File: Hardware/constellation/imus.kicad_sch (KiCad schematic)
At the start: 8 parts, among them U2 ICM-45686, U3 LSM6DSV32X

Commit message: shift to hierarchial design, add GNSS, mag, accel
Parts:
- removed C1, C2, C3, C4: 100nF, Capacitor_SMD:C_0402_1005Metric, symbol Device:C_Small
- removed R1, R2: 10K, Resistor_SMD:R_0402_1005Metric_Pad0.72x0.64mm_HandSolder, symbol Device:R_Small
- removed U2: ICM-45686, ICM_45686:IC_ICM-45686, symbol ICM-45686:ICM-45686
- removed U3: LSM6DSV32X, Package_LGA:LGA-14_3x2.5mm_P0.5mm_LayoutBorder3x4y, symbol Sensor_Motion:LSM6DSL
- added C16, C17, C18, C19: 100nF, Capacitor_SMD:C_0402_1005Metric, symbol Device:C_Small
- added R11, R12: 10K, Resistor_SMD:R_0402_1005Metric_Pad0.72x0.64mm_HandSolder, symbol Device:R_Small
- added U11: ICM-45686, ICM_45686:IC_ICM-45686, symbol ICM-45686:ICM-45686
- added U12: LSM6DSV32X, Package_LGA:LGA-14_3x2.5mm_P0.5mm_LayoutBorder3x4y, symbol Sensor_Motion:LSM6DSL
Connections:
- net GND: now also C16.2, C17.2, C18.2, C19.2, U11.10 (RESV), U11.11 (RESV), U11.2 (RESV), U11.3 (RESV), U11.6 (GND), U11.7 (RESV), U12.2 (SDX), U12.3 (SCX), U12.6 (GND), U12.7 (GND)
- net ICM_CS: now also R12.2, U11.12 (AP_CS)
- net ICM_INT1: now also U11.4 (INT1/INT), U12.4 (INT1)
- net ICM_INT2: now also U11.9 (INT2/CLKIN), U12.9 (INT2)
- net ICM_MISO: now also U11.1 (AP_SDO)
- net ICM_MOSI: now also U11.14 (AP_SDIO/AP_SDI)
- net ICM_SCK: now also U11.13 (AP_SCLK)
- net LSM6_CS: now also R11.2, U12.12 (CS)
- net LSM6_MISO: now also U12.1 (SDO/SA0)
- net LSM6_MOSI: now also U12.14 (SDA)
- net LSM6_SCK: now also U12.13 (SCL)
- net VDD: now also C16.1, C17.1, C18.1, C19.1, R11.1, R12.1, U11.5 (VDDIO), U11.8 (VDD), U12.5 (VDDIO), U12.8 (VDD)

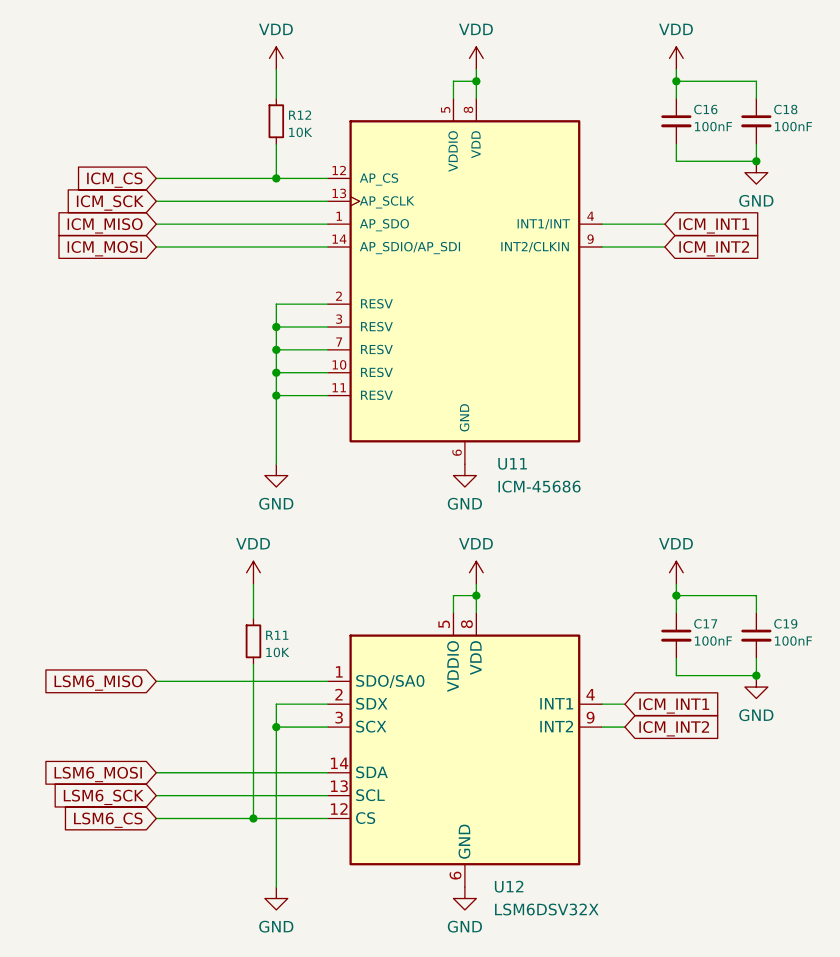
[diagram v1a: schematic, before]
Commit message: add the hierarchal pins to the imu block
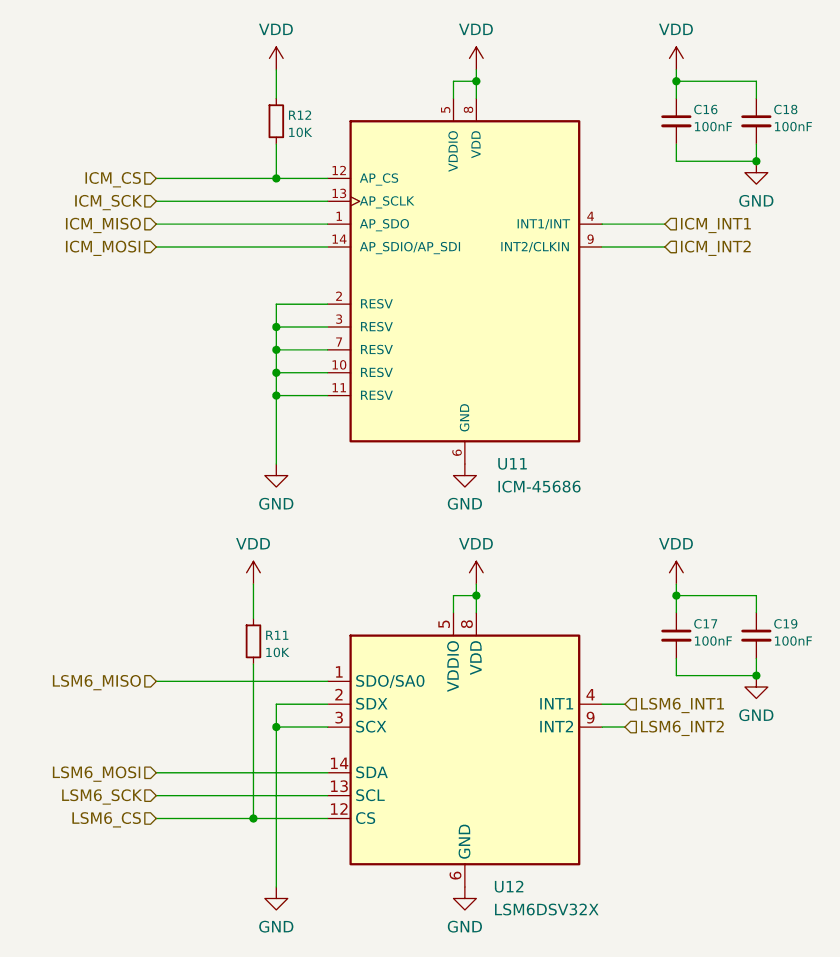
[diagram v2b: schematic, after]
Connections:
- net ICM_INT1: no longer U12.4 (INT1)
- net ICM_INT2: no longer U12.9 (INT2)
- new net LSM6_INT1: U12.4 (INT1)
- new net LSM6_INT2: U12.9 (INT2)
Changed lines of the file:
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@@
 		)
 	)
-	(global_label "ICM_SCK"
+	(hierarchical_label "ICM_SCK"
 		(shape input)
 		(at 113.03 73.66 180)
-		(fields_autoplaced yes)
 		(effects
 			(font
@@
 			(justify right)
 		)
-		(property "Intersheetrefs" "${INTERSHEET_REFS}"
-			(at 94.0187 73.66 0)
-			(hide yes)
-			(show_name no)
-			(do_not_autoplace no)
-			(effects
-				(font
-					(size 1.27 1.27)
-				)
-				(justify right)
-			)
-		)
 	)
-	(global_label "LSM6_SCK"
+	(hierarchical_label "LSM6_SCK"
 		(shape input)
 		(at 113.03 139.7 180)
-		(fields_autoplaced yes)
 		(effects
 			(font
@@
 			(justify right)
 		)
-		(property "Intersheetrefs" "${INTERSHEET_REFS}"
-			(at 94.0187 139.7 0)
-			(hide yes)
-			(show_name no)
-			(do_not_autoplace no)
-			(effects
-				(font
-					(size 1.27 1.27)
-				)
-				(justify right)
-			)
-		)
 	)
-	(global_label "ICM_INT2"
+	(hierarchical_label "LSM6_INT2"
 		(shape input)
-		(at 169.545 78.74 0)
-		(fields_autoplaced yes)
+		(at 165.1 132.08 0)
 		(effects
 			(font
@@
 			(justify left)
 		)
-		(property "Intersheetrefs" "${INTERSHEET_REFS}"
-			(at 188.5563 78.74 0)
-			(hide yes)
-			(show_name no)
-			(do_not_autoplace no)
-			(effects
-				(font
-					(size 1.27 1.27)
-				)
-				(justify left)
-			)
-		)
 	)
-	(global_label "LSM6_MISO"
+	(hierarchical_label "ICM_MOSI"
 		(shape input)
-		(at 113.03 127 180)
-		(fields_autoplaced yes)
+		(at 113.03 78.74 180)
 		(effects
 			(font
@@
 			(justify right)
 		)
-		(property "Intersheetrefs" "${INTERSHEET_REFS}"
-			(at 94.0187 127 0)
-			(hide yes)
-			(show_name no)
-			(do_not_autoplace no)
-			(effects
-				(font
-					(size 1.27 1.27)
-				)
-				(justify right)
-			)
-		)
 	)
-	(global_label "ICM_MOSI"
+	(hierarchical_label "LSM6_MOSI"
 		(shape input)
-		(at 113.03 78.74 180)
-		(fields_autoplaced yes)
+		(at 113.03 137.16 180)
 		(effects
 			(font
@@
 			(justify right)
 		)
-		(property "Intersheetrefs" "${INTERSHEET_REFS}"
-			(at 94.0187 78.74 0)
-			(hide yes)
-			(show_name no)
-			(do_not_autoplace no)
-			(effects
-				(font
-					(size 1.27 1.27)
-				)
-				(justify right)
+	)
+	(hierarchical_label "ICM_CS"
+		(shape input)
+		(at 113.03 71.12 180)
+		(effects
+			(font
+				(size 1.27 1.27)
 			)
+			(justify right)
 		)
 	)
-	(global_label "ICM_INT1"
+	(hierarchical_label "LSM6_INT1"
 		(shape input)
-		(at 169.545 76.2 0)
-		(fields_autoplaced yes)
+		(at 165.1 129.54 0)
 		(effects
 			(font
@@
 			(justify left)
 		)
-		(property "Intersheetrefs" "${INTERSHEET_REFS}"
-			(at 188.5563 76.2 0)
-			(hide yes)
-			(show_name no)
-			(do_not_autoplace no)
-			(effects
-				(font
-					(size 1.27 1.27)
-				)
-				(justify left)
+	)
+	(hierarchical_label "ICM_INT1"
+		(shape input)
+		(at 169.545 76.2 0)
+		(effects
+			(font
+				(size 1.27 1.27)
 			)
+			(justify left)
 		)
 	)
-	(global_label "LSM6_CS"
+	(hierarchical_label "ICM_MISO"
 		(shape input)
-		(at 113.03 142.24 180)
-		(fields_autoplaced yes)
+		(at 113.03 76.2 180)
 		(effects
 			(font
@@
 			(justify right)
 		)
-		(property "Intersheetrefs" "${INTERSHEET_REFS}"
-			(at 94.0187 142.24 0)
-			(hide yes)
-			(show_name no)
-			(do_not_autoplace no)
-			(effects
-				(font
-					(size 1.27 1.27)
-				)
-				(justify right)
-			)
-		)
 	)
-	(global_label "ICM_CS"
+	(hierarchical_label "LSM6_MISO"
 		(shape input)
-		(at 113.03 71.12 180)
-		(fields_autoplaced yes)
+		(at 113.03 127 180)
 		(effects
 			(font
@@
 			(justify right)
 		)
-		(property "Intersheetrefs" "${INTERSHEET_REFS}"
-			(at 94.0187 71.12 0)
-			(hide yes)
-			(show_name no)
-			(do_not_autoplace no)
-			(effects
-				(font
-					(size 1.27 1.27)
-				)
-				(justify right)
+	)
+	(hierarchical_label "LSM6_CS"
+		(shape input)
+		(at 113.03 142.24 180)
+		(effects
+			(font
+				(size 1.27 1.27)
 			)
+			(justify right)
 		)
 	)
-	(global_label "ICM_INT1"
+	(hierarchical_label "ICM_INT2"
 		(shape input)
-		(at 165.1 129.54 0)
-		(fields_autoplaced yes)
+		(at 169.545 78.74 0)
 		(effects
 			(font
@@
 			(justify left)
 		)
-		(property "Intersheetrefs" "${INTERSHEET_REFS}"
-			(at 184.1113 129.54 0)
-			(hide yes)
-			(show_name no)
-			(do_not_autoplace no)
-			(effects
-				(font
-					(size 1.27 1.27)
-				)
-				(justify left)
-			)
-		)
 	)
-	(global_label "LSM6_MOSI"
-		(shape input)
-		(at 113.03 137.16 180)
-		(fields_autoplaced yes)
-		(effects
-			(font
-				(size 1.27 1.27)
-			)
-			(justify right)
-		)
-		(property "Intersheetrefs" "${INTERSHEET_REFS}"
-			(at 94.0187 137.16 0)
-			(hide yes)
-			(show_name no)
-			(do_not_autoplace no)
-			(effects
-				(font
-					(size 1.27 1.27)
-				)
-				(justify right)
-			)
-		)
-	)
-	(global_label "ICM_INT2"
-		(shape input)
-		(at 165.1 132.08 0)
-		(fields_autoplaced yes)
-		(effects
-			(font
-				(size 1.27 1.27)
-			)
-			(justify left)
-		)
-		(property "Intersheetrefs" "${INTERSHEET_REFS}"
-			(at 184.1113 132.08 0)
-			(hide yes)
-			(show_name no)
-			(do_not_autoplace no)
-			(effects
-				(font
-					(size 1.27 1.27)
-				)
-				(justify left)
-			)
-		)
-	)
-	(global_label "ICM_MISO"
-		(shape input)
-		(at 113.03 76.2 180)
-		(fields_autoplaced yes)
-		(effects
-			(font
-				(size 1.27 1.27)
-			)
-			(justify right)
-		)
-		(property "Intersheetrefs" "${INTERSHEET_REFS}"
-			(at 94.0187 76.2 0)
-			(hide yes)
-			(show_name no)
-			(do_not_autoplace no)
-			(effects
-				(font
-					(size 1.27 1.27)
-				)
-				(justify right)
-			)
-		)
-	)

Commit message: add lr2021 footprint and comms
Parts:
- renumbered C16 to C1, C17 to C2, C18 to C3, C19 to C4, R11 to R1, R12 to R2, U11 to U2, U12 to U3
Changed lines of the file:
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@@
 		(in_pos_files yes)
 		(dnp no)
-		(property "Reference" "C17"
+		(property "Reference" "C2"
 			(at 172.72 120.65 0)
 			(show_name no)
@@
 			(project "constellation"
 				(path "/ba226b81-7f6b-4f1e-964f-d5311904768c/c727e166-794d-46fa-ba85-5f8ee24b890e"
-					(reference "C17")
+					(reference "C2")
 					(unit 1)
 				)
@@
 		(dnp no)
 		(fields_autoplaced yes)
-		(property "Reference" "#PWR040"
+		(property "Reference" "#PWR01"
 			(at 123.825 120.015 0)
 			(hide yes)
@@
 			(project "constellation"
 				(path "/ba226b81-7f6b-4f1e-964f-d5311904768c/c727e166-794d-46fa-ba85-5f8ee24b890e"
-					(reference "#PWR040")
+					(reference "#PWR01")
 					(unit 1)
 				)
@@
 		(in_pos_files yes)
 		(dnp no)
-		(property "Reference" "C19"
+		(property "Reference" "C4"
 			(at 181.61 120.65 0)
 			(show_name no)
@@
 			(project "constellation"
 				(path "/ba226b81-7f6b-4f1e-964f-d5311904768c/c727e166-794d-46fa-ba85-5f8ee24b890e"
-					(reference "C19")
+					(reference "C4")
 					(unit 1)
 				)
@@
 		(dnp no)
 		(fields_autoplaced yes)
-		(property "Reference" "#PWR048"
+		(property "Reference" "#PWR09"
 			(at 170.815 62.865 0)
 			(hide yes)
@@
 			(project "constellation"
 				(path "/ba226b81-7f6b-4f1e-964f-d5311904768c/c727e166-794d-46fa-ba85-5f8ee24b890e"
-					(reference "#PWR048")
+					(reference "#PWR09")
 					(unit 1)
 				)
@@
 		(dnp no)
 		(fields_autoplaced yes)
-		(property "Reference" "#PWR045"
+		(property "Reference" "#PWR06"
 			(at 147.32 156.21 0)
 			(hide yes)
@@
 			(project "constellation"
 				(path "/ba226b81-7f6b-4f1e-964f-d5311904768c/c727e166-794d-46fa-ba85-5f8ee24b890e"
-					(reference "#PWR045")
+					(reference "#PWR06")
 					(unit 1)
 				)
@@
 		(dnp no)
 		(fields_autoplaced yes)
-		(property "Reference" "U11"
+		(property "Reference" "U2"
 			(at 150.876 102.87 0)
 			(show_name no)
@@
 			(project "constellation"
 				(path "/ba226b81-7f6b-4f1e-964f-d5311904768c/c727e166-794d-46fa-ba85-5f8ee24b890e"
-					(reference "U11")
+					(reference "U2")
 					(unit 1)
 				)
@@
 		(in_pos_files yes)
 		(dnp no)
-		(property "Reference" "R12"
+		(property "Reference" "R2"
 			(at 127.635 64.1351 0)
 			(show_name no)
@@
 			(project "constellation"
 				(path "/ba226b81-7f6b-4f1e-964f-d5311904768c/c727e166-794d-46fa-ba85-5f8ee24b890e"
-					(reference "R12")
+					(reference "R2")
 					(unit 1)
 				)
@@
 		(in_pos_files yes)
 		(dnp no)
-		(property "Reference" "#PWR047"
+		(property "Reference" "#PWR08"
 			(at 148.59 120.015 0)
 			(hide yes)
@@
 			(project "constellation"
 				(path "/ba226b81-7f6b-4f1e-964f-d5311904768c/c727e166-794d-46fa-ba85-5f8ee24b890e"
-					(reference "#PWR047")
+					(reference "#PWR08")
 					(unit 1)
 				)
@@
 		(in_pos_files yes)
 		(dnp no)
-		(property "Reference" "C16"
+		(property "Reference" "C1"
 			(at 172.72 63.5 0)
 			(show_name no)
@@
 			(project "constellation"
 				(path "/ba226b81-7f6b-4f1e-964f-d5311904768c/c727e166-794d-46fa-ba85-5f8ee24b890e"
-					(reference "C16")
+					(reference "C1")
 					(unit 1)
 				)
@@
 		(in_pos_files yes)
 		(dnp no)
-		(property "Reference" "C18"
+		(property "Reference" "C3"
 			(at 181.61 63.5 0)
 			(show_name no)
@@
 			(project "constellation"
 				(path "/ba226b81-7f6b-4f1e-964f-d5311904768c/c727e166-794d-46fa-ba85-5f8ee24b890e"
-					(reference "C18")
+					(reference "C3")
 					(unit 1)
 				)
@@
 		(in_pos_files yes)
 		(dnp no)
-		(property "Reference" "R11"
+		(property "Reference" "R1"
 			(at 125.095 121.9201 0)
 			(show_name no)
@@
 			(project "constellation"
 				(path "/ba226b81-7f6b-4f1e-964f-d5311904768c/c727e166-794d-46fa-ba85-5f8ee24b890e"
-					(reference "R11")
+					(reference "R1")
 					(unit 1)
 				)
@@
 		(dnp no)
 		(fields_autoplaced yes)
-		(property "Reference" "#PWR051"
+		(property "Reference" "#PWR012"
 			(at 179.705 132.715 0)
 			(hide yes)
@@
 			(project "constellation"
 				(path "/ba226b81-7f6b-4f1e-964f-d5311904768c/c727e166-794d-46fa-ba85-5f8ee24b890e"
-					(reference "#PWR051")
+					(reference "#PWR012")
 					(unit 1)
 				)
@@
 		(dnp no)
 		(fields_autoplaced yes)
-		(property "Reference" "#PWR043"
+		(property "Reference" "#PWR04"
 			(at 126.365 156.21 0)
 			(hide yes)
@@
 			(project "constellation"
 				(path "/ba226b81-7f6b-4f1e-964f-d5311904768c/c727e166-794d-46fa-ba85-5f8ee24b890e"
-					(reference "#PWR043")
+					(reference "#PWR04")
 					(unit 1)
 				)
@@
 		(dnp no)
 		(fields_autoplaced yes)
-		(property "Reference" "#PWR049"
+		(property "Reference" "#PWR010"
 			(at 170.815 120.015 0)
 			(hide yes)
@@
 			(project "constellation"
 				(path "/ba226b81-7f6b-4f1e-964f-d5311904768c/c727e166-794d-46fa-ba85-5f8ee24b890e"
-					(reference "#PWR049")
+					(reference "#PWR010")
 					(unit 1)
 				)
@@
 		(dnp no)
 		(fields_autoplaced yes)
-		(property "Reference" "#PWR050"
+		(property "Reference" "#PWR011"
 			(at 179.705 75.565 0)
 			(hide yes)
@@
 			(project "constellation"
 				(path "/ba226b81-7f6b-4f1e-964f-d5311904768c/c727e166-794d-46fa-ba85-5f8ee24b890e"
-					(reference "#PWR050")
+					(reference "#PWR011")
 					(unit 1)
 				)
@@
 		(dnp no)
 		(fields_autoplaced yes)
-		(property "Reference" "#PWR042"
+		(property "Reference" "#PWR03"
 			(at 126.365 109.22 0)
 			(hide yes)
@@
 			(project "constellation"
 				(path "/ba226b81-7f6b-4f1e-964f-d5311904768c/c727e166-794d-46fa-ba85-5f8ee24b890e"
-					(reference "#PWR042")
+					(reference "#PWR03")
 					(unit 1)
 				)
@@
 		(dnp no)
 		(fields_autoplaced yes)
-		(property "Reference" "#PWR041"
+		(property "Reference" "#PWR02"
 			(at 126.365 62.865 0)
 			(hide yes)
@@
 			(project "constellation"
 				(path "/ba226b81-7f6b-4f1e-964f-d5311904768c/c727e166-794d-46fa-ba85-5f8ee24b890e"
-					(reference "#PWR041")
+					(reference "#PWR02")
 					(unit 1)
 				)
@@
 		(dnp no)
 		(fields_autoplaced yes)
-		(property "Reference" "#PWR044"
+		(property "Reference" "#PWR05"
 			(at 147.32 109.22 0)
 			(hide yes)
@@
 			(project "constellation"
 				(path "/ba226b81-7f6b-4f1e-964f-d5311904768c/c727e166-794d-46fa-ba85-5f8ee24b890e"
-					(reference "#PWR044")
+					(reference "#PWR05")
 					(unit 1)
 				)
@@
 		(in_pos_files yes)
 		(dnp no)
-		(property "Reference" "#PWR046"
+		(property "Reference" "#PWR07"
 			(at 148.59 62.865 0)
 			(hide yes)
@@
 			(project "constellation"
 				(path "/ba226b81-7f6b-4f1e-964f-d5311904768c/c727e166-794d-46fa-ba85-5f8ee24b890e"
-					(reference "#PWR046")
+					(reference "#PWR07")
 					(unit 1)
 				)
@@
 		(in_pos_files yes)
 		(dnp no)
-		(property "Reference" "U12"
+		(property "Reference" "U3"
 			(at 150.495 149.86 0)
 			(show_name no)
@@
 			(project "constellation"
 				(path "/ba226b81-7f6b-4f1e-964f-d5311904768c/c727e166-794d-46fa-ba85-5f8ee24b890e"
-					(reference "U12")
-					(unit 1)
-				)
+					(reference "U3")
+					(unit 1)
+				)

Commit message: add pyro stuff, start system power
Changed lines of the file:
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@@
 	)
 	(hierarchical_label "LSM6_INT2"
-		(shape input)
+		(shape output)
 		(at 165.1 132.08 0)
 		(effects
@@
 	)
 	(hierarchical_label "LSM6_INT1"
-		(shape input)
+		(shape output)
 		(at 165.1 129.54 0)
 		(effects
@@
 	)
 	(hierarchical_label "ICM_INT1"
-		(shape input)
+		(shape output)
 		(at 169.545 76.2 0)
 		(effects
@@
 	)
 	(hierarchical_label "ICM_MISO"
-		(shape input)
+		(shape output)
 		(at 113.03 76.2 180)
 		(effects
@@
 	)
 	(hierarchical_label "LSM6_MISO"
-		(shape input)
+		(shape output)
 		(at 113.03 127 180)
 		(effects
@@
 	)
 	(hierarchical_label "ICM_INT2"
-		(shape input)
+		(shape output)
 		(at 169.545 78.74 0)
 		(effects
